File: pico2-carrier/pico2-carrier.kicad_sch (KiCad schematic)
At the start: 24 parts, among them IC1 TFDU4101-TT3, IC2 M95512-DWDW4TP_K, IC3 W25Q128JVSIM_TR, SW1 RUN, U1 Pico 2

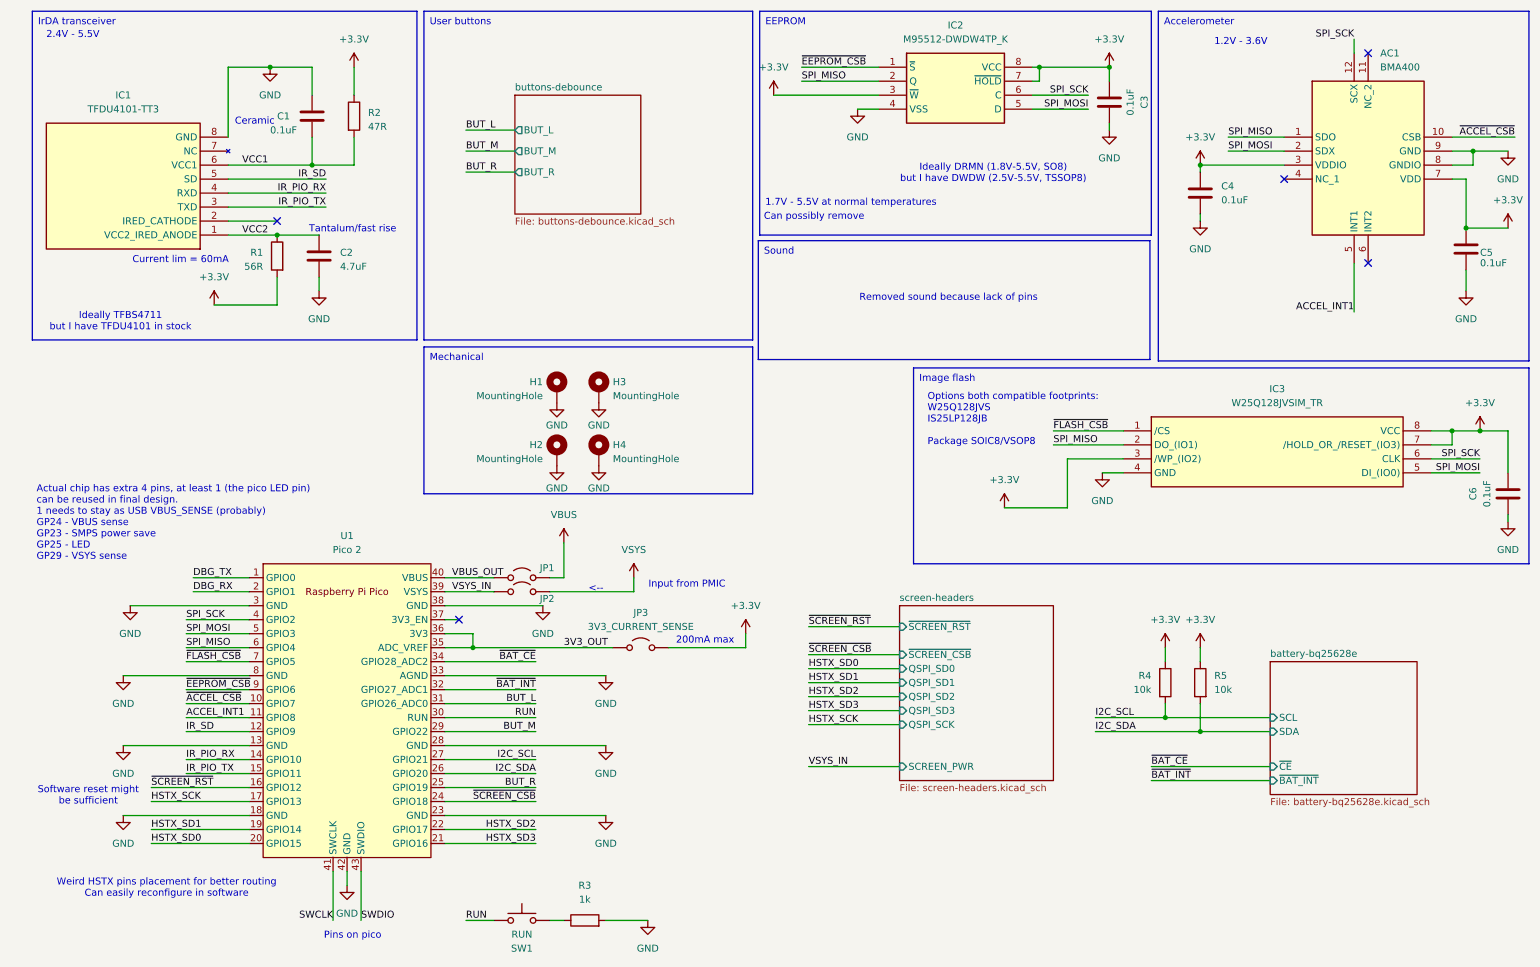
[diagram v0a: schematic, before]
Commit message: carrier: add some improvements to eeprom
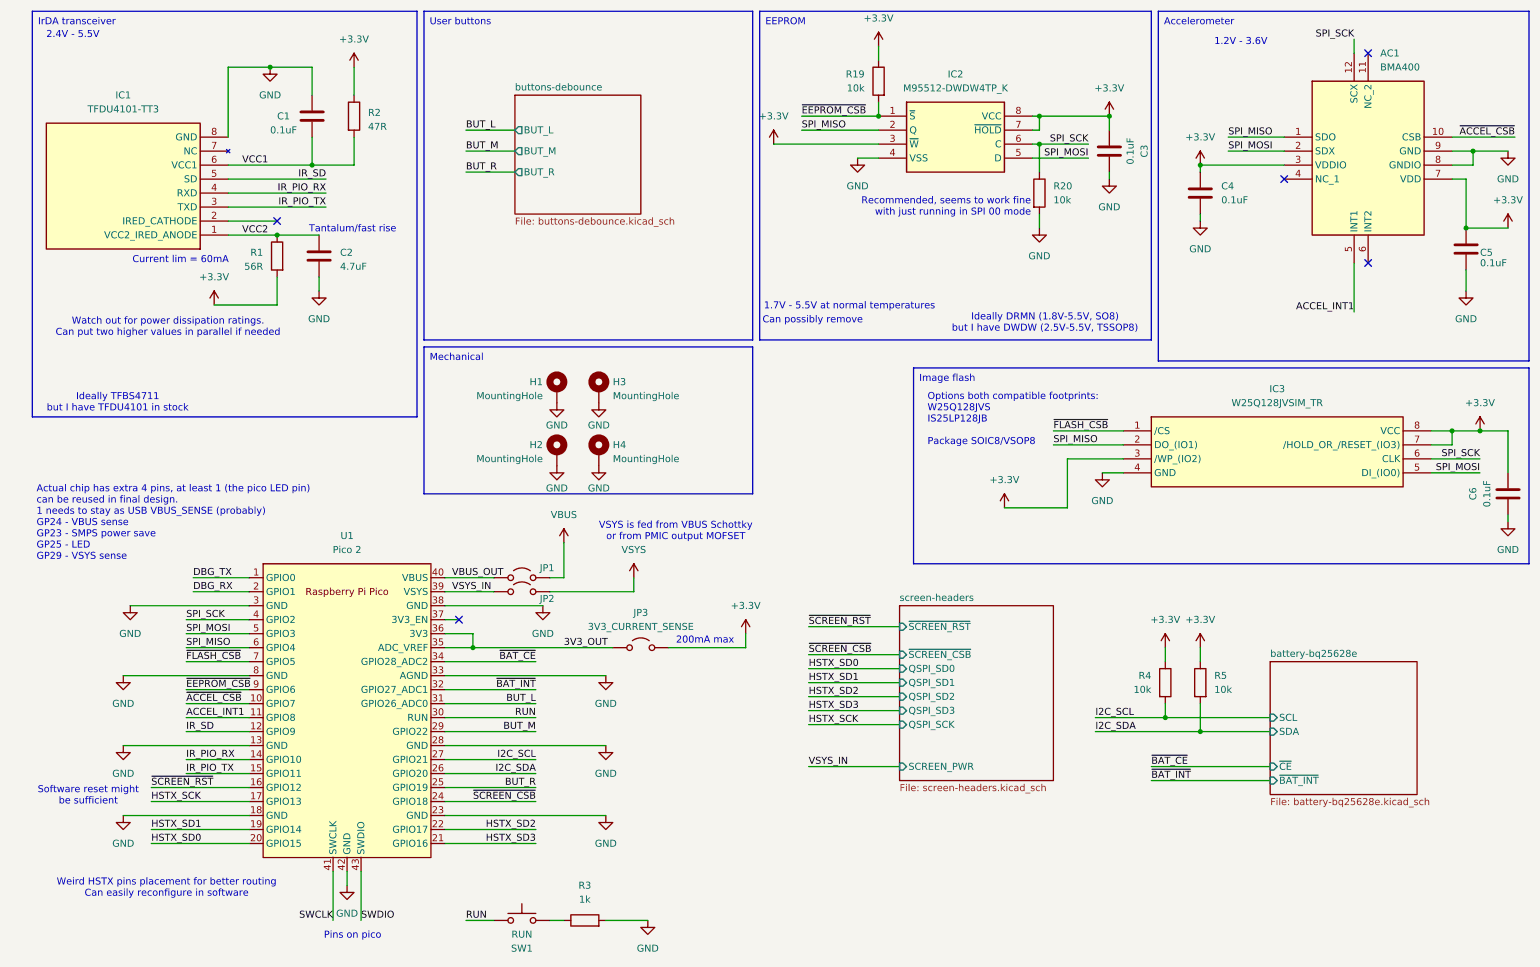
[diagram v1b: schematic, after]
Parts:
- added R19, R20: 10k, symbol Device:R
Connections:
- net +3.3V: now also R19.1
- net GND: now also R20.2
- net SPI_SCK: now also R20.1
- net ~{EEPROM_CSB}: now also R19.2
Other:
- note added: "Recommended, seems to work fine with just running in SPI 00 mode"
- note added: "VSYS is fed from VBUS Schottky or from PMIC output MOFSET"
- note added: "Watch out for power dissipation ratings. Can put two higher values in parallel if needed"
- note removed: "<--"
- note removed: "Ceramic"
- note removed: "Input from PMIC"
- note removed: "Removed sound because lack of pins"
- moved on the sheet: C3, IC2
